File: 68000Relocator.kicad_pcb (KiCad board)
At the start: 2 copper layers, 97.5 x 97.4 mm, 2 parts, among them U1 68000D, U2 68000D

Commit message: Fix tracks
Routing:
- net /A14: track 45.9 -> 47.7 mm
- net /A21: track 102.9 -> 103.8 mm
- net /A17: track 62.0 -> 62.8 mm
- net /A19: track 71.4 -> 72.1 mm
- net /A20: track 78.6 -> 79.2 mm

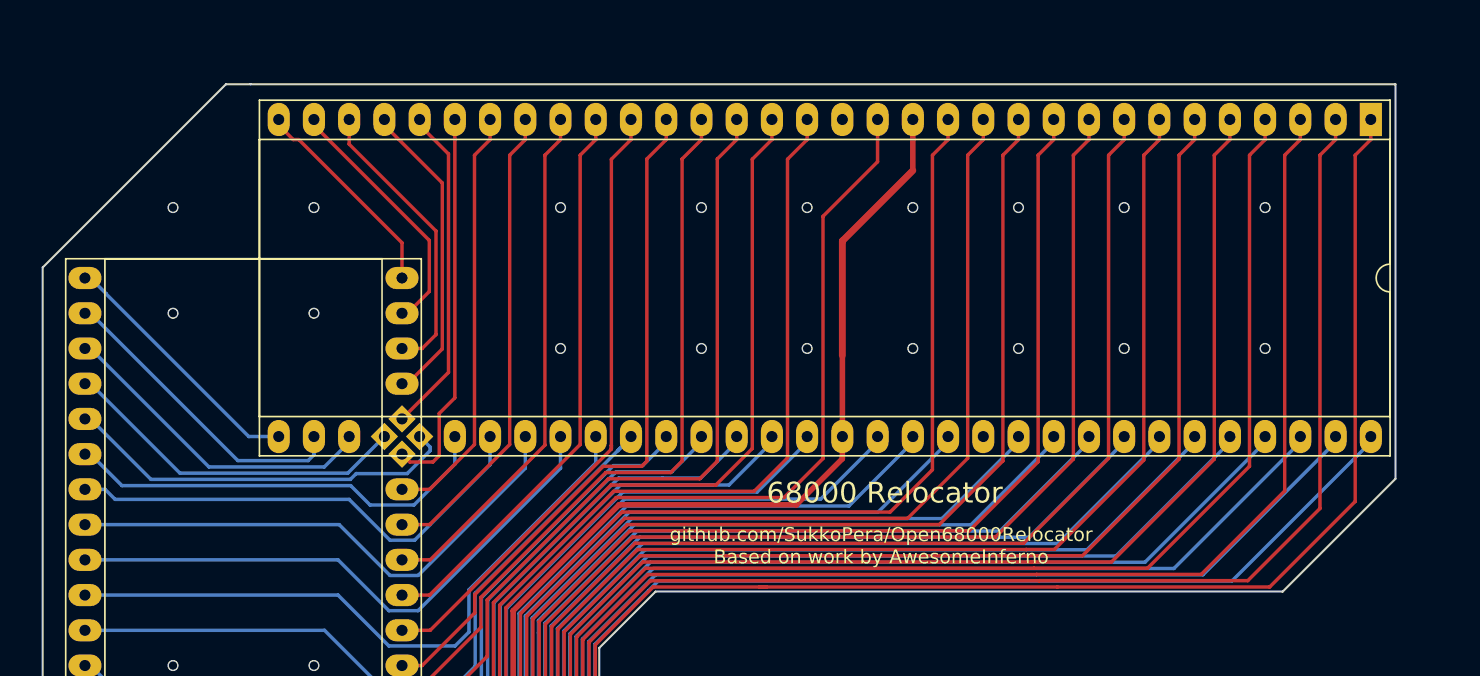
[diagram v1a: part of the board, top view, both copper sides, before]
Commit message: Make board "square" and other minor fixes
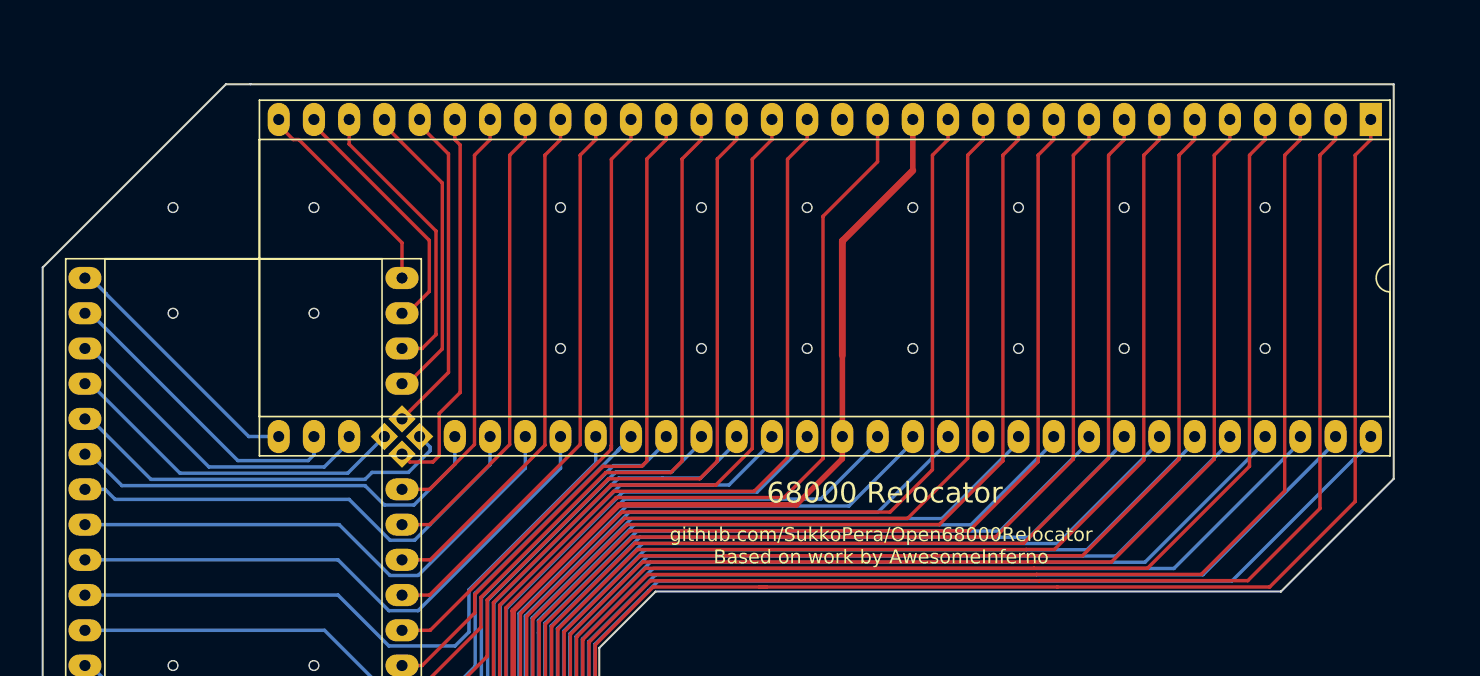
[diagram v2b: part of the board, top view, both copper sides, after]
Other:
- board size 97.5 x 97.4 mm -> 97.4 x 97.4 mm
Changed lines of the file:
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@@
     (thickness 1.6)
     (drawings 17)
-    (tracks 596)
+    (tracks 598)
     (zones 0)
     (modules 2)
@@
   )
   (gr_line (start 121.158 144.653) (end 129.286 136.525) (layer Edge.Cuts) (width 0.15))
-  (dimension 97.536 (width 0.3) (layer F.Fab)
-    (gr_text "97,536 mm" (at 137.922 39.429) (layer F.Fab)
+  (dimension 97.409 (width 0.3) (layer F.Fab)
+    (gr_text "97,409 mm" (at 137.8585 39.429) (layer F.Fab)
       (effects (font (size 1.5 1.5) (thickness 0.3)))
     )
-    (feature1 (pts (xy 186.69 47.244) (xy 186.69 40.942579)))
+    (feature1 (pts (xy 186.563 47.244) (xy 186.563 40.942579)))
     (feature2 (pts (xy 89.154 47.244) (xy 89.154 40.942579)))
-    (crossbar (pts (xy 89.154 41.529) (xy 186.69 41.529)))
-    (arrow1a (pts (xy 186.69 41.529) (xy 185.563496 42.115421)))
-    (arrow1b (pts (xy 186.69 41.529) (xy 185.563496 40.942579)))
+    (crossbar (pts (xy 89.154 41.529) (xy 186.563 41.529)))
+    (arrow1a (pts (xy 186.563 41.529) (xy 185.436496 42.115421)))
+    (arrow1b (pts (xy 186.563 41.529) (xy 185.436496 40.942579)))
     (arrow2a (pts (xy 89.154 41.529) (xy 90.280504 42.115421)))
     (arrow2b (pts (xy 89.154 41.529) (xy 90.280504 40.942579)))
@@
   )
   (gr_line (start 129.286 87.884) (end 133.35 83.82) (layer Edge.Cuts) (width 0.15))
-  (gr_line (start 178.562 83.82) (end 186.69 75.692) (layer Edge.Cuts) (width 0.15))
-  (gr_line (start 133.35 83.82) (end 178.562 83.82) (layer Edge.Cuts) (width 0.15))
+  (gr_line (start 178.435 83.82) (end 186.563 75.692) (layer Edge.Cuts) (width 0.15))
+  (gr_line (start 133.35 83.82) (end 178.435 83.82) (layer Edge.Cuts) (width 0.15))
   (gr_line (start 129.286 136.525) (end 129.286 87.884) (layer Edge.Cuts) (width 0.15))
   (gr_line (start 102.362 47.244) (end 104.14 47.244) (layer Edge.Cuts) (width 0.15))
   (gr_line (start 89.154 60.452) (end 102.362 47.244) (layer Edge.Cuts) (width 0.15))
   (gr_line (start 121.158 144.653) (end 89.154 144.653) (layer Edge.Cuts) (width 0.15))
-  (gr_line (start 186.69 47.244) (end 186.69 75.692) (layer Edge.Cuts) (width 0.15))
-  (gr_line (start 104.14 47.244) (end 186.69 47.244) (layer Edge.Cuts) (width 0.15))
+  (gr_line (start 186.563 47.244) (end 186.563 75.692) (layer Edge.Cuts) (width 0.15))
+  (gr_line (start 104.14 47.244) (end 186.563 47.244) (layer Edge.Cuts) (width 0.15))
   (gr_line (start 89.154 144.653) (end 89.154 60.452) (layer Edge.Cuts) (width 0.15))
   (gr_text "github.com/SukkoPera/Open68000Relocator\nBased on work by AwesomeInferno" (at 149.606 80.518) (layer F.SilkS)
@@
   (segment (start 173.62699 74.27701) (end 166.218266 81.685734) (width 0.25) (layer F.Cu) (net 9) (status 40000))
   (segment (start 160.443999 81.685734) (end 160.4386 81.691133) (width 0.25) (layer F.Cu) (net 9) (status 40000))
-  (segment (start 92.602 71.374) (end 92.202 71.374) (width 0.25) (layer B.Cu) (net 10))
-  (segment (start 96.961527 75.733527) (end 92.602 71.374) (width 0.25) (layer B.Cu) (net 10))
-  (segment (start 111.757805 75.314606) (end 111.338884 75.733527) (width 0.25) (layer B.Cu) (net 10))
-  (segment (start 115.439394 75.314606) (end 111.757805 75.314606) (width 0.25) (layer B.Cu) (net 10))
-  (segment (start 117.094 73.66) (end 115.439394 75.314606) (width 0.25) (layer B.Cu) (net 10) (status 40000))
-  (segment (start 111.338884 75.733527) (end 96.961527 75.733527) (width 0.25) (layer B.Cu) (net 10))
   (segment (start 116.332 72.644) (end 116.332 72.898) (width 0.25) (layer F.Cu) (net 10))
-  (segment (start 117.094 73.406) (end 116.332 72.644) (width 0.25) (layer B.Cu) (net 10) (status 40000))
-  (segment (start 117.094 73.66) (end 117.094 73.406) (width 0.25) (layer B.Cu) (net 10) (status 40000))
+  (segment (start 117.094 73.406) (end 116.332 72.644) (width 0.25) (layer B.Cu) (net 10))
+  (segment (start 92.202 71.374) (end 92.602 71.374) (width 0.25) (layer B.Cu) (net 10))
+  (segment (start 92.602 71.374) (end 96.961527 75.733527) (width 0.25) (layer B.Cu) (net 10))
+  (segment (start 117.094 73.66) (end 117.094 73.406) (width 0.25) (layer B.Cu) (net 10))
+  (segment (start 112.903 75.228959) (end 115.525041 75.228959) (width 0.25) (layer B.Cu) (net 10))
+  (segment (start 96.961527 75.733527) (end 112.398432 75.733527) (width 0.25) (layer B.Cu) (net 10))
+  (segment (start 112.398432 75.733527) (end 112.903 75.228959) (width 0.25) (layer B.Cu) (net 10))
+  (segment (start 115.525041 75.228959) (end 117.094 73.66) (width 0.25) (layer B.Cu) (net 10))
   (segment (start 115.462 127.254) (end 115.062 127.254) (width 0.25) (layer F.Cu) (net 11) (status 40000))
   (segment (start 126.751885 115.964115) (end 115.462 127.254) (width 0.25) (layer F.Cu) (net 11) (status 40000))
@@
   (segment (start 171.08699 74.27701) (end 164.128277 81.235723) (width 0.25) (layer F.Cu) (net 11) (status 40000))
   (segment (start 160.257599 81.235723) (end 160.2522 81.241122) (width 0.25) (layer F.Cu) (net 11) (status 40000))
-  (segment (start 118.872 72.644) (end 118.872 74.635004) (width 0.25) (layer B.Cu) (net 12) (status 40000))
-  (segment (start 118.872 74.635004) (end 115.927994 77.57901) (width 0.25) (layer B.Cu) (net 12) (status 40000))
-  (segment (start 115.927994 77.57901) (end 112.760239 77.57901) (width 0.25) (layer B.Cu) (net 12))
-  (segment (start 112.760239 77.57901) (end 111.364766 76.183537) (width 0.25) (layer B.Cu) (net 12))
-  (segment (start 111.364766 76.183537) (end 94.871537 76.183537) (width 0.25) (layer B.Cu) (net 12))
-  (segment (start 94.871537 76.183537) (end 92.602 73.914) (width 0.25) (layer B.Cu) (net 12))
-  (segment (start 92.602 73.914) (end 92.202 73.914) (width 0.25) (layer B.Cu) (net 12))
+  (segment (start 118.872 74.635004) (end 118.872 72.644) (width 0.25) (layer B.Cu) (net 12))
+  (segment (start 92.202 73.914) (end 92.602 73.914) (width 0.25) (layer B.Cu) (net 12))
+  (segment (start 92.602 73.914) (end 94.871537 76.183537) (width 0.25) (layer B.Cu) (net 12))
+  (segment (start 94.871537 76.183537) (end 112.396527 76.183537) (width 0.25) (layer B.Cu) (net 12))
+  (segment (start 112.396527 76.183537) (end 113.792 77.57901) (width 0.25) (layer B.Cu) (net 12))
+  (segment (start 113.792 77.57901) (end 115.927994 77.57901) (width 0.25) (layer B.Cu) (net 12))
+  (segment (start 115.927994 77.57901) (end 118.872 74.635004) (width 0.25) (layer B.Cu) (net 12))
   (segment (start 115.462 124.714) (end 115.062 124.714) (width 0.25) (layer F.Cu) (net 13) (status 40000))
   (segment (start 126.301874 113.874126) (end 115.462 124.714) (width 0.25) (layer F.Cu) (net 13) (status 40000))
@@
   (segment (start 126.268434 86.487) (end 126.268434 132.295106) (width 0.25) (layer B.Cu) (net 50))
   (segment (start 126.268434 132.295106) (end 119.75254 138.811) (width 0.25) (layer B.Cu) (net 50))
-  (segment (start 117.74699 70.97501) (end 118.872 69.85) (width 0.25) (layer F.Cu) (net 51) (status 40000))
-  (segment (start 118.872 69.85) (end 118.872 49.784) (width 0.25) (layer F.Cu) (net 51) (status 40000))
-  (segment (start 117.290316 74.479684) (end 117.74699 74.02301) (width 0.25) (layer F.Cu) (net 51))
-  (segment (start 117.74699 74.02301) (end 117.74699 70.97501) (width 0.25) (layer F.Cu) (net 51))
-  (segment (start 115.062 73.914) (end 115.627684 74.479684) (width 0.25) (layer F.Cu) (net 51))
-  (segment (start 115.627684 74.479684) (end 117.290316 74.479684) (width 0.25) (layer F.Cu) (net 51))
+  (segment (start 115.627684 74.479684) (end 115.062 73.914) (width 0.25) (layer F.Cu) (net 51))
+  (segment (start 117.290316 74.479684) (end 115.627684 74.479684) (width 0.25) (layer F.Cu) (net 51))
+  (segment (start 118.872 49.784) (end 118.872 51.234) (width 0.25) (layer F.Cu) (net 51))
+  (segment (start 118.872 51.234) (end 119.253 51.615) (width 0.25) (layer F.Cu) (net 51))
+  (segment (start 119.253 69.469) (end 117.74699 70.97501) (width 0.25) (layer F.Cu) (net 51))
+  (segment (start 117.74699 70.97501) (end 117.74699 74.02301) (width 0.25) (layer F.Cu) (net 51))
+  (segment (start 119.253 51.615) (end 119.253 69.469) (width 0.25) (layer F.Cu) (net 51))
+  (segment (start 117.74699 74.02301) (end 117.290316 74.479684) (width 0.25) (layer F.Cu) (net 51))
   (segment (start 99.31682 141.478) (end 95.562287 137.723467) (width 0.25) (layer B.Cu) (net 52) (status 40000))
   (segment (start 95.562287 130.214287) (end 92.602 127.254) (width 0.25) (layer B.Cu) (net 52) (status 40000))

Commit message: Ready for release
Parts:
- added P99: OSHW_LOGO, Symbol:OSHW-Logo_11.4x12mm_Copper, B.Cu at (172.1, 61.0)
- U1: footprint Housings_DIP:DIP-64_W22.86mm_Socket_LongPads -> Open68000Relocator:DIP-64_W22.86mm_Socket_LongPads_Socket
- U2: footprint Housings_DIP:DIP-64_W22.86mm_Socket_LongPads -> Open68000Relocator:DIP-64_W22.86mm_Socket_LongPads_IC
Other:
- board text added: "Open 68000 Relocator"
- board text removed: "68000 Relocator"
